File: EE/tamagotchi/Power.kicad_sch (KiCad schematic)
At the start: 7 parts, among them J8 Conn_01x02_Male, P1 USB_C_Plug_USB2.0

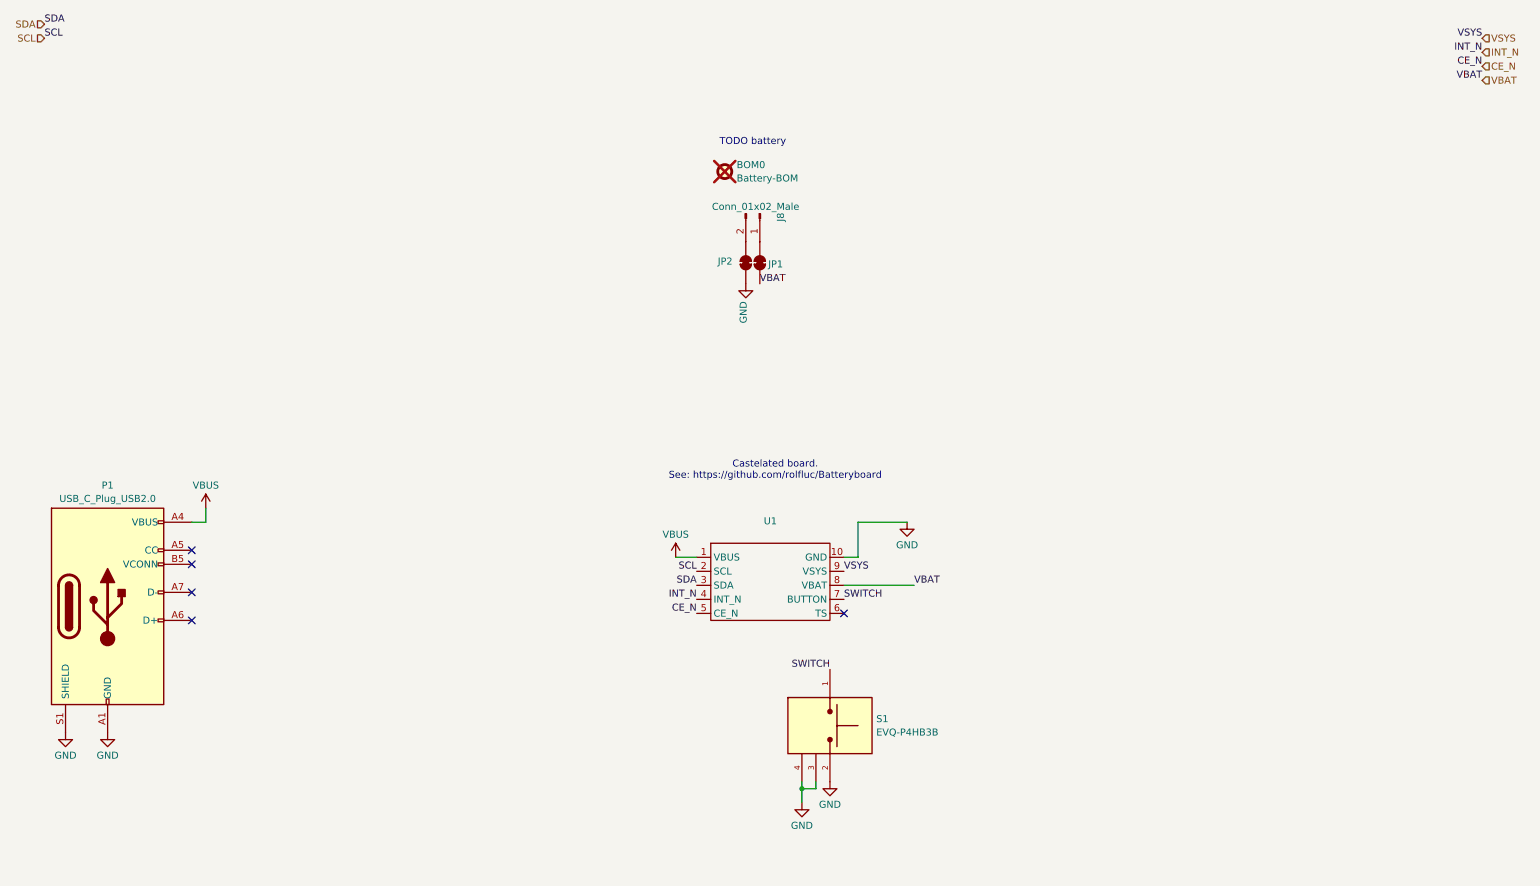
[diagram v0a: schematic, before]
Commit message: WIP - Overall Cleanup, Power Change
Added expected loads for power in schematic.
Changed power arch to use existing design that appears to work.
Removed rear backlight LEDs - shouldn't be necessary.
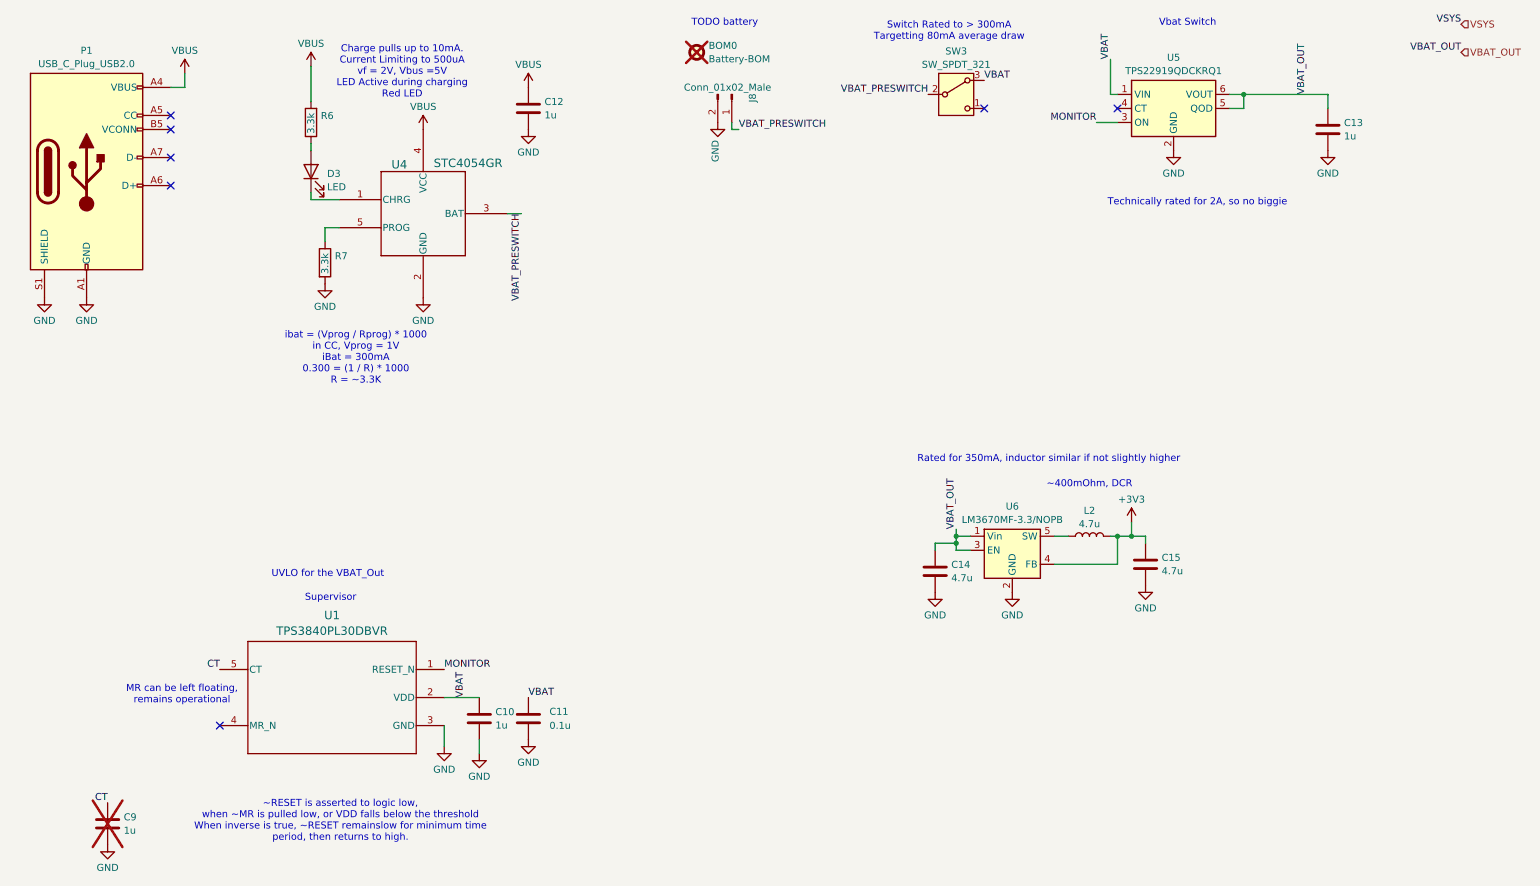
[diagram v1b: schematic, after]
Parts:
- removed JP1, JP2: SolderJumper_2_Bridged, Jumper:SolderJumper-2_P1.3mm_Bridged2Bar_RoundedPad1.0x1.5mm, symbol Jumper:SolderJumper_2_Bridged
- removed S1: EVQ-P4HB3B, Library:SW_EVQ-P4HB3B, symbol New_Library:EVQ-P4HB3B
- removed U1: ~, Library:BatteryBoard, symbol New_Library:bq_castelated
- added C10, C12, C13, C9: 1u, Capacitor_SMD:C_0402_1005Metric_Pad0.74x0.62mm_HandSolder, symbol Device:C
- added C11: 0.1u, Capacitor_SMD:C_0402_1005Metric_Pad0.74x0.62mm_HandSolder, symbol Device:C
- added C14, C15: 4.7u, Capacitor_SMD:C_0603_1608Metric, symbol Device:C
- added D3: LED, Library:LED_0604, symbol Device:LED
- added L2: 4.7u, Inductor_SMD:L_0805_2012Metric, symbol Device:L
- added R6, R7: 3.3k, Resistor_SMD:R_0402_1005Metric_Pad0.72x0.64mm_HandSolder, symbol Device:R
- added SW3: SW_SPDT_321, Library:EGJ1210, symbol Switch:SW_SPDT_321
- added U1: TPS3840PL30DBVR, Package_TO_SOT_SMD:SC-74A-5_1.55x2.9mm_P0.95mm, symbol New_Library:TPS3840PH30DBVR
- added U4: STC4054GR, Package_TO_SOT_SMD:TSOT-23-5, symbol New_Library:STC4054GR
- added U5: TPS22919QDCKRQ1, Package_TO_SOT_SMD:SOT-363_SC-70-6, symbol Power_Management:TPS22917DBV
- added U6: LM3670MF-3.3/NOPB, Package_TO_SOT_SMD:TSOT-23-5, symbol Regulator_Switching:LM3670MF
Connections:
- net GND: now also J8.2 (Pin_2), C10.2, C11.2, C12.2, C13.2, C14.2, C15.2, C9.2, R7.2, U1.3 (GND), U4.2 (GND), U5.2 (GND), U6.2 (GND)
- net VBAT: now also C10.1, C11.1, SW3.3 (A), U1.2 (VDD), U5.1 (VIN)
- net VBUS: now also C12.1, R6.2, U4.4 (VCC)
- net VBAT_PRESWITCH: now reaches J8.1 (Pin_1)
- net VBAT_PRESWITCH: now also SW3.2 (B), U4.3 (BAT)
- new net: L2.1, U6.5 (SW)
- new net: D3.1 (K), U4.1 (CHRG)
- new net: D3.2 (A), R6.1
- new net: R7.1, U4.5 (PROG)
- new net +3V3: C15.1, L2.2, U6.4 (FB)
- new net CT: C9.1, U1.5 (CT)
- new net MONITOR: U1.1 (RESET_N), U5.3 (ON)
- new net VBAT_OUT: C13.1, C14.1, U5.5 (QOD), U5.6 (VOUT), U6.1 (Vin), U6.3 (EN)
- no-connect marks 5 -> 7
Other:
- note added: "Charge pulls up to 10mA. Current Limiting to 500uA vf = 2V, Vbus =5V LED Active during charging Red LED"
- note added: "MR can be left floating, remains operational"
- note added: "Rated for 350mA, inductor similar if not slightly higher"
- note added: "Supervisor"
- note added: "Switch Rated to > 300mA Targetting 80mA average draw"
- note added: "Technically rated for 2A, so no biggie"
- note added: "UVLO for the VBAT_Out"
- note added: "Vbat Switch"
- note added: "ibat = (Vprog / Rprog) * 1000 in CC, Vprog = 1V iBat = 300mA 0.300 = (1 / R) * 1000 R = ~3.3K"
- note added: "~400mOhm, DCR"
- note added: "~RESET is asserted to logic low, when ~MR is pulled low, or VDD falls below the threshold When inverse is true, ~RESET remainslow for minimum time period, then returns to high."
- note removed: "Castelated board. See: https://github.com/rolfluc/Batteryboard"
- moved on the sheet: BOM0, J8, P1

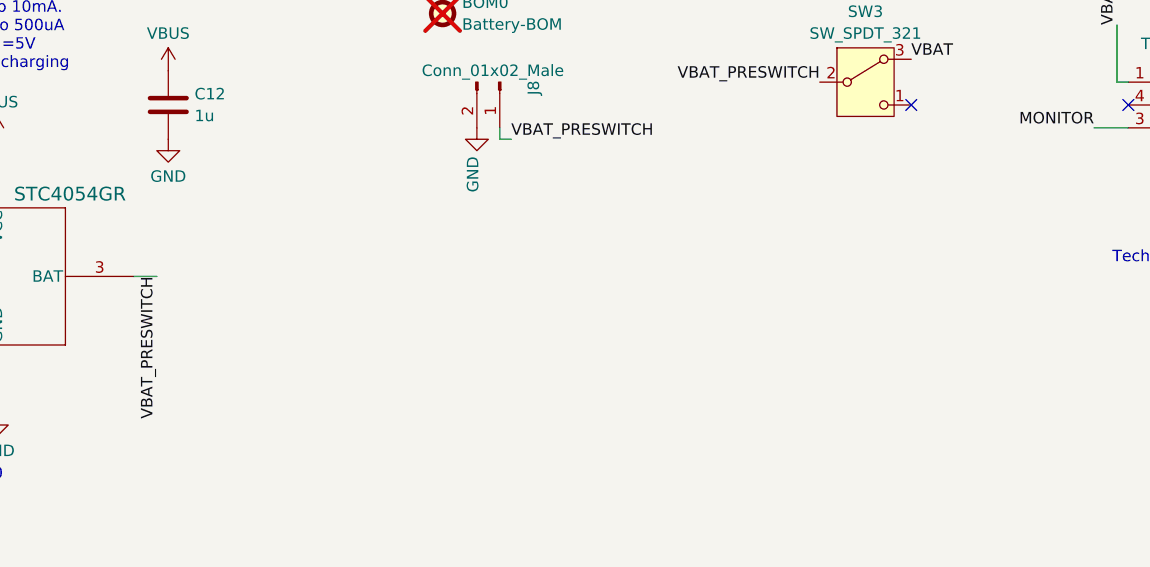
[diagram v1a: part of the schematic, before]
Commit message: Partial Migration to a different topology of battery control
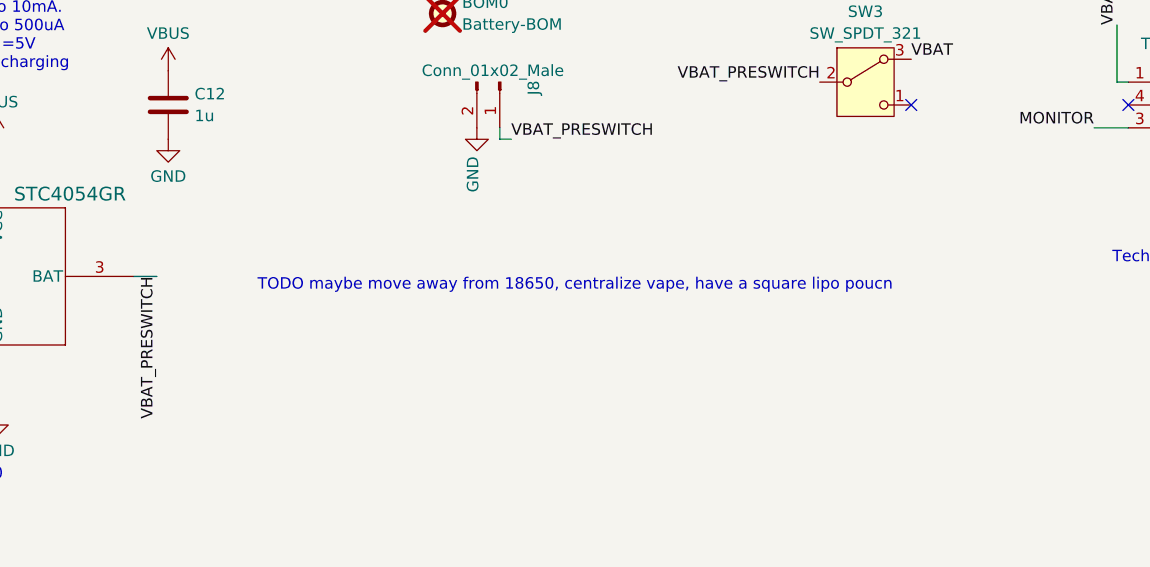
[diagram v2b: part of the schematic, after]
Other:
- note added: "TODO maybe move away from 18650, centralize vape, have a square lipo poucn"
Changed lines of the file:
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@@
+		)
+	)
+	(text "TODO maybe move away from 18650, centralize vape, have a square lipo poucn"
+		(exclude_from_sim no)
+		(at 150.622 50.546 0)
+		(effects
+			(font
+				(size 1.27 1.27)
+			)
 		)
 	)
